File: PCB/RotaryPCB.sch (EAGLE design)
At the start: 4 parts

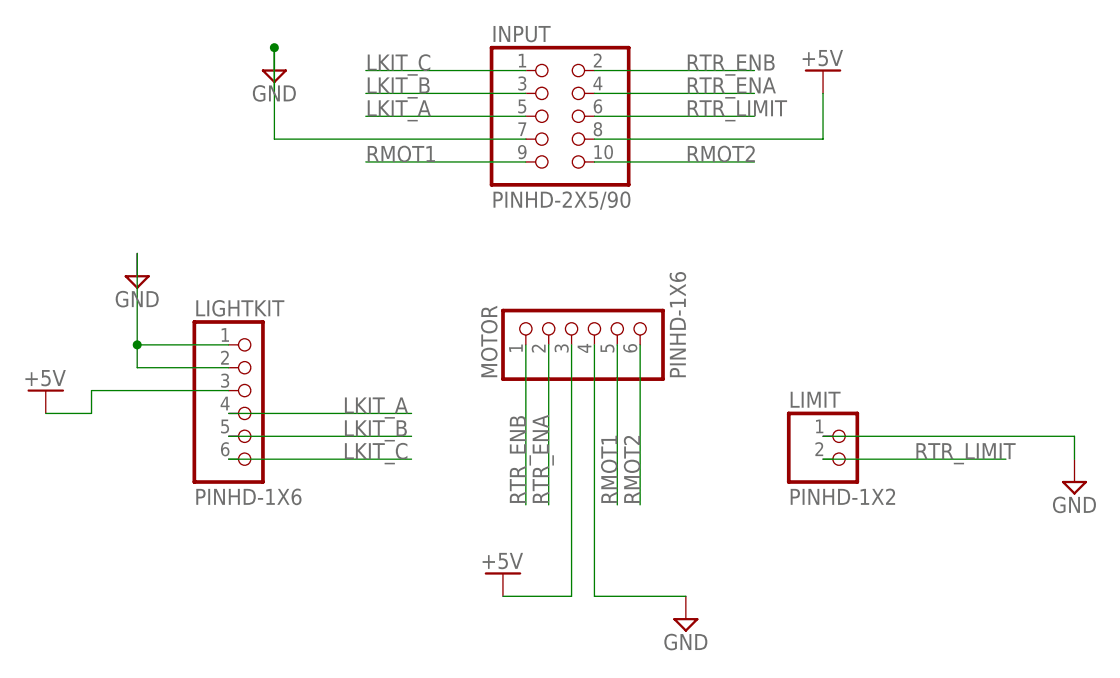
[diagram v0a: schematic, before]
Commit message: This version uses thicker traces and adds a copper pour. The lifter board is a four layer board. The order of the connection pins on the rotary has changed. Do NOT use the same cable as the older board. The order was changed to allow using a silicone ribbon cable.
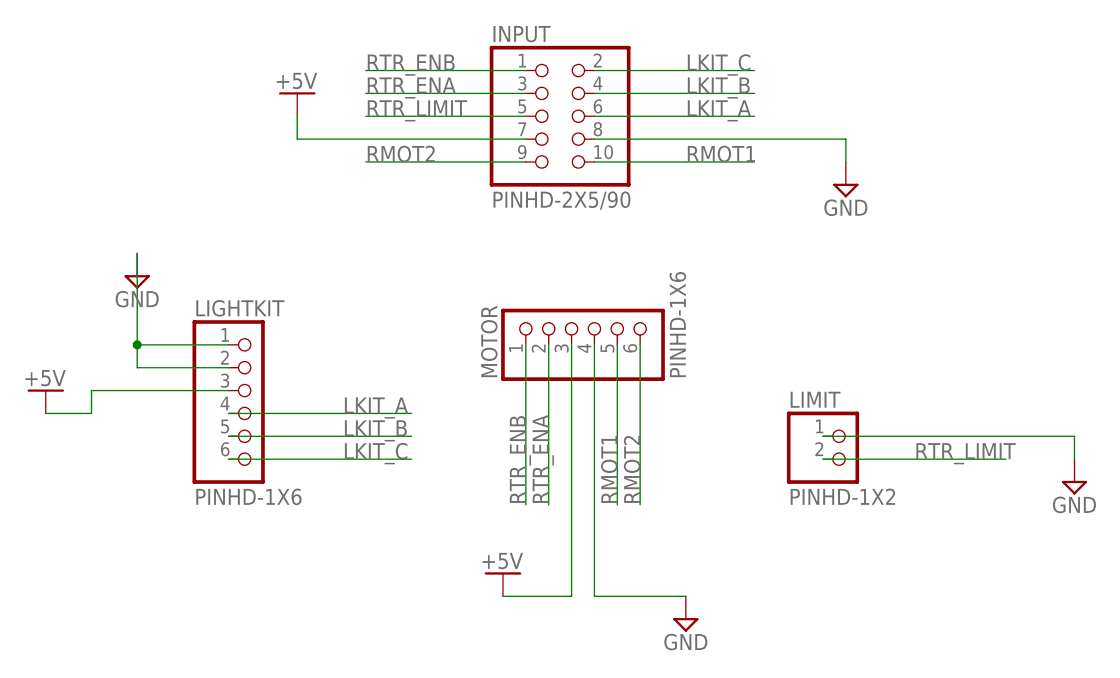
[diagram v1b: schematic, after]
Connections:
- net +5V: now also INPUT.7; no longer INPUT.8
- net GND: now also INPUT.8; no longer INPUT.7
- net LKIT_A: now also INPUT.6; no longer INPUT.5
- net LKIT_B: now also INPUT.4; no longer INPUT.3
- net LKIT_C: now also INPUT.2; no longer INPUT.1
- net RMOT1: now also INPUT.10; no longer INPUT.9
- net RMOT2: now also INPUT.9; no longer INPUT.10
- net RTR_ENA: now also INPUT.3; no longer INPUT.4
- net RTR_ENB: now also INPUT.1; no longer INPUT.2
- net RTR_LIMIT: now also INPUT.5; no longer INPUT.6
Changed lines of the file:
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@@
 <class number="0" name="default" width="0" drill="0">
+</class>
+<class number="1" name="Motor Power" width="0.6096" drill="0">
+</class>
+<class number="2" name="5VPower" width="0.4064" drill="0">
 </class>
 </classes>
@@
 <part name="SUPPLY2" library="Power_Symbols" deviceset="+5V" device="" value="+5V"/>
 <part name="SUPPLY4" library="Power_Symbols" deviceset="GND" device="" value="GND"/>
-<part name="SUPPLY3" library="Power_Symbols" deviceset="+5V" device="" value="+5V"/>
-<part name="SUPPLY7" library="Power_Symbols" deviceset="GND" device="" value="GND"/>
 <part name="SUPPLY6" library="Power_Symbols" deviceset="GND" device="" value="GND"/>
 <part name="SUPPLY1" library="Power_Symbols" deviceset="+5V" device="" value="+5V"/>
 <part name="SUPPLY5" library="Power_Symbols" deviceset="GND" device="" value="GND"/>
 <part name="FRAME1" library="frames" library_urn="urn:adsk.eagle:library:229" deviceset="DINA5_L" device=""/>
+<part name="SUPPLY3" library="Power_Symbols" deviceset="+5V" device="" value="+5V"/>
+<part name="SUPPLY7" library="Power_Symbols" deviceset="GND" device="" value="GND"/>
 </parts>
 <sheets>
@@
 <attribute name="VALUE" x="76.2" y="27.94" size="1.778" layer="96" align="center"/>
 </instance>
-<instance part="SUPPLY3" gate="G$1" x="91.44" y="88.9" smashed="yes">
-<attribute name="VALUE" x="91.313" y="91.948" size="1.778" layer="96" align="bottom-center"/>
-</instance>
-<instance part="SUPPLY7" gate="G$1" x="30.48" y="91.44" smashed="yes">
-<attribute name="VALUE" x="30.48" y="88.9" size="1.778" layer="96" align="center"/>
-</instance>
 <instance part="SUPPLY6" gate="G$1" x="119.38" y="45.72" smashed="yes">
 <attribute name="VALUE" x="119.38" y="43.18" size="1.778" layer="96" align="center"/>
@@
 <attribute name="SHEET" x="126.365" y="-2.54" size="2.54" layer="94"/>
 </instance>
+<instance part="SUPPLY3" gate="G$1" x="33.02" y="86.36" smashed="yes">
+<attribute name="VALUE" x="32.893" y="89.408" size="1.778" layer="96" align="bottom-center"/>
+</instance>
+<instance part="SUPPLY7" gate="G$1" x="93.98" y="78.74" smashed="yes">
+<attribute name="VALUE" x="93.98" y="76.2" size="1.778" layer="96" align="center"/>
+</instance>
 </instances>
 <busses>
 </busses>
 <nets>
-<net name="GND" class="0">
+<net name="GND" class="2">
 <segment>
 <pinref part="MOTOR" gate="A" pin="4"/>
@@
 <wire x1="66.04" y1="33.02" x2="76.2" y2="33.02" width="0.1524" layer="91"/>
 <pinref part="SUPPLY4" gate="G$1" pin="GND"/>
-</segment>
-<segment>
-<wire x1="30.48" y1="88.9" x2="30.48" y2="93.98" width="0.1524" layer="91"/>
-<pinref part="SUPPLY7" gate="G$1" pin="GND"/>
-<pinref part="INPUT" gate="A" pin="7"/>
-<wire x1="58.42" y1="83.82" x2="30.48" y2="83.82" width="0.1524" layer="91"/>
-<wire x1="30.48" y1="83.82" x2="30.48" y2="93.98" width="0.1524" layer="91"/>
-<junction x="30.48" y="93.98"/>
 </segment>
 <segment>
@@
 <junction x="15.24" y="60.96"/>
 </segment>
-</net>
-<net name="+5V" class="0">
+<segment>
+<pinref part="INPUT" gate="A" pin="8"/>
+<wire x1="66.04" y1="83.82" x2="93.98" y2="83.82" width="0.1524" layer="91"/>
+<wire x1="93.98" y1="83.82" x2="93.98" y2="81.28" width="0.1524" layer="91"/>
+<pinref part="SUPPLY7" gate="G$1" pin="GND"/>
+</segment>
+</net>
+<net name="+5V" class="2">
 <segment>
 <pinref part="MOTOR" gate="A" pin="3"/>
@@
 </segment>
 <segment>
-<pinref part="INPUT" gate="A" pin="8"/>
-<wire x1="66.04" y1="83.82" x2="91.44" y2="83.82" width="0.1524" layer="91"/>
+<pinref part="INPUT" gate="A" pin="7"/>
+<wire x1="58.42" y1="83.82" x2="33.02" y2="83.82" width="0.1524" layer="91"/>
+<wire x1="33.02" y1="83.82" x2="33.02" y2="86.36" width="0.1524" layer="91"/>
 <pinref part="SUPPLY3" gate="G$1" pin="+5V"/>
-<wire x1="91.44" y1="83.82" x2="91.44" y2="88.9" width="0.1524" layer="91"/>
-</segment>
-</net>
-<net name="RMOT2" class="0">
+</segment>
+</net>
+<net name="RMOT2" class="1">
 <segment>
 <pinref part="MOTOR" gate="A" pin="6"/>
@@
 </segment>
 <segment>
+<pinref part="INPUT" gate="A" pin="9"/>
+<wire x1="58.42" y1="81.28" x2="40.64" y2="81.28" width="0.1524" layer="91"/>
+<label x="40.64" y="81.28" size="1.778" layer="95"/>
+</segment>
+</net>
+<net name="RMOT1" class="1">
+<segment>
+<pinref part="MOTOR" gate="A" pin="5"/>
+<wire x1="68.58" y1="60.96" x2="68.58" y2="43.18" width="0.1524" layer="91"/>
+<label x="68.58" y="43.18" size="1.778" layer="95" rot="R90"/>
+</segment>
+<segment>
 <pinref part="INPUT" gate="A" pin="10"/>
 <wire x1="66.04" y1="81.28" x2="83.82" y2="81.28" width="0.1524" layer="91"/>
@@
 </segment>
 </net>
-<net name="RMOT1" class="0">
-<segment>
-<pinref part="MOTOR" gate="A" pin="5"/>
-<wire x1="68.58" y1="60.96" x2="68.58" y2="43.18" width="0.1524" layer="91"/>
-<label x="68.58" y="43.18" size="1.778" layer="95" rot="R90"/>
-</segment>
-<segment>
-<pinref part="INPUT" gate="A" pin="9"/>
-<wire x1="58.42" y1="81.28" x2="40.64" y2="81.28" width="0.1524" layer="91"/>
-<label x="40.64" y="81.28" size="1.778" layer="95"/>
-</segment>
-</net>
 <net name="RTR_LIMIT" class="0">
+<segment>
+<pinref part="LIMIT" gate="G$1" pin="2"/>
+<wire x1="91.44" y1="48.26" x2="111.76" y2="48.26" width="0.1524" layer="91"/>
+<label x="101.6" y="48.26" size="1.778" layer="95"/>
+</segment>
+<segment>
+<pinref part="INPUT" gate="A" pin="5"/>
+<wire x1="58.42" y1="86.36" x2="40.64" y2="86.36" width="0.1524" layer="91"/>
+<label x="40.64" y="86.36" size="1.778" layer="95"/>
+</segment>
+</net>
+<net name="LKIT_B" class="0">
+<segment>
+<pinref part="LIGHTKIT" gate="A" pin="5"/>
+<wire x1="25.4" y1="50.8" x2="45.72" y2="50.8" width="0.1524" layer="91"/>
+<label x="38.1" y="50.8" size="1.778" layer="95"/>
+</segment>
+<segment>
+<pinref part="INPUT" gate="A" pin="4"/>
+<wire x1="66.04" y1="88.9" x2="83.82" y2="88.9" width="0.1524" layer="91"/>
+<label x="76.2" y="88.9" size="1.778" layer="95"/>
+</segment>
+</net>
+<net name="LKIT_C" class="0">
+<segment>
+<pinref part="LIGHTKIT" gate="A" pin="6"/>
+<wire x1="25.4" y1="48.26" x2="45.72" y2="48.26" width="0.1524" layer="91"/>
+<label x="38.1" y="48.26" size="1.778" layer="95"/>
+</segment>
+<segment>
+<pinref part="INPUT" gate="A" pin="2"/>
+<wire x1="66.04" y1="91.44" x2="83.82" y2="91.44" width="0.1524" layer="91"/>
+<label x="76.2" y="91.44" size="1.778" layer="95"/>
+</segment>
+</net>
+<net name="LKIT_A" class="0">
+<segment>
+<pinref part="LIGHTKIT" gate="A" pin="4"/>
+<wire x1="25.4" y1="53.34" x2="45.72" y2="53.34" width="0.1524" layer="91"/>
+<label x="38.1" y="53.34" size="1.778" layer="95"/>
+</segment>
 <segment>
 <pinref part="INPUT" gate="A" pin="6"/>
@@
 <label x="76.2" y="86.36" size="1.778" layer="95"/>
 </segment>
-<segment>
-<pinref part="LIMIT" gate="G$1" pin="2"/>
-<wire x1="91.44" y1="48.26" x2="111.76" y2="48.26" width="0.1524" layer="91"/>
-<label x="101.6" y="48.26" size="1.778" layer="95"/>
-</segment>
-</net>
-<net name="LKIT_B" class="0">
-<segment>
-<pinref part="LIGHTKIT" gate="A" pin="5"/>
-<wire x1="25.4" y1="50.8" x2="45.72" y2="50.8" width="0.1524" layer="91"/>
-<label x="38.1" y="50.8" size="1.778" layer="95"/>
+</net>
+<net name="RTR_ENA" class="0">
+<segment>
+<pinref part="MOTOR" gate="A" pin="2"/>
+<wire x1="60.96" y1="60.96" x2="60.96" y2="43.18" width="0.1524" layer="91"/>
+<label x="60.96" y="43.18" size="1.778" layer="95" rot="R90"/>
 </segment>
 <segment>
@@
 </segment>
 </net>
-<net name="LKIT_C" class="0">
-<segment>
-<pinref part="LIGHTKIT" gate="A" pin="6"/>
-<wire x1="25.4" y1="48.26" x2="45.72" y2="48.26" width="0.1524" layer="91"/>
-<label x="38.1" y="48.26" size="1.778" layer="95"/>
+<net name="RTR_ENB" class="0">
+<segment>
+<pinref part="MOTOR" gate="A" pin="1"/>
+<wire x1="58.42" y1="60.96" x2="58.42" y2="43.18" width="0.1524" layer="91"/>
+<label x="58.42" y="43.18" size="1.778" layer="95" rot="R90"/>
 </segment>
 <segment>
@@
 </segment>
 </net>
-<net name="LKIT_A" class="0">
-<segment>
-<pinref part="INPUT" gate="A" pin="5"/>
-<wire x1="58.42" y1="86.36" x2="40.64" y2="86.36" width="0.1524" layer="91"/>
-<label x="40.64" y="86.36" size="1.778" layer="95"/>
-</segment>
-<segment>
-<pinref part="LIGHTKIT" gate="A" pin="4"/>
-<wire x1="25.4" y1="53.34" x2="45.72" y2="53.34" width="0.1524" layer="91"/>
-<label x="38.1" y="53.34" size="1.778" layer="95"/>
-</segment>
-</net>
-<net name="RTR_ENA" class="0">
-<segment>
-<pinref part="MOTOR" gate="A" pin="2"/>
-<wire x1="60.96" y1="60.96" x2="60.96" y2="43.18" width="0.1524" layer="91"/>
-<label x="60.96" y="43.18" size="1.778" layer="95" rot="R90"/>
-</segment>
-<segment>
-<pinref part="INPUT" gate="A" pin="4"/>
-<wire x1="66.04" y1="88.9" x2="83.82" y2="88.9" width="0.1524" layer="91"/>
-<label x="76.2" y="88.9" size="1.778" layer="95"/>
-</segment>
-</net>
-<net name="RTR_ENB" class="0">
-<segment>
-<pinref part="MOTOR" gate="A" pin="1"/>
-<wire x1="58.42" y1="60.96" x2="58.42" y2="43.18" width="0.1524" layer="91"/>
-<label x="58.42" y="43.18" size="1.778" layer="95" rot="R90"/>
-</segment>
-<segment>
-<pinref part="INPUT" gate="A" pin="2"/>
-<wire x1="66.04" y1="91.44" x2="83.82" y2="91.44" width="0.1524" layer="91"/>
-<label x="76.2" y="91.44" size="1.778" layer="95"/>
-</segment>
-</net>
